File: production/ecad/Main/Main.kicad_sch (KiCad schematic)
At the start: 1 part, among them J1 61204021621

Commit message: touches to schem
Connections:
- net 3.3v: now reaches J1.1
- net 3.3v: now also J1.17
- net ANO_SW2: now reaches J1.10
- net LCD_CS: now reaches J1.11
- net ANO_SW3: now reaches J1.12
- net GND: now reaches J1.14
- net GND: now also J1.20, J1.25, J1.30, J1.34, J1.39, J1.6, J1.9
- net ANO_SW4: now reaches J1.16
- net ANO_SW5: now reaches J1.18
- net LCD_DIN: now reaches J1.19
- net 5v: now reaches J1.2
- net 5v: now also J1.4
- net MISO: now reaches J1.21
- net ANO_ENCB: now reaches J1.22
- net LCD_CLK: now reaches J1.23
- net ANO_ENCA: now reaches J1.24
- net LCD_DS: now reaches J1.27
- net LCD_BL: now reaches J1.29
- net SDA: now reaches J1.3
- net LCD_RST: now reaches J1.31
- net MTR_IN1: now reaches J1.32
- net MTR_IN1: now also J1.33
- net VBR_MTR_EN2: now reaches J1.37
- net VBR_MTR_EN2: now also J1.40
- net VBR_MTR_EN1: now reaches J1.38
- net SCL: now reaches J1.5
- net ANO_SW1: now reaches J1.8
- no-connect marks 0 -> 16
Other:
- added sheet ANO Dial (../Peripheral/Peripheral.kicad_sch)
- added sheet LCD (../LCD/LCD.kicad_sch)
- added sheet Motor (../Motor/Motor.kicad_sch)
- note added: "EXTERNAL GROUND PROVIDED FROM BMS/WALL"
- note added: "EXTERNAL VOLTAGE PROVIDED BY BMS/WALL"
- note added: "On pinout: - LCD screen - Motor driver - Rotary dial - Vibration motors"
- note added: "Still need: - weight sensor - ADC (maybe) -"
- moved on the sheet: J1

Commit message: schematic draft merged w neha
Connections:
- net VBR_MTR_EN2 is gone; now on net GND: J1.37, J1.40
- net MTR_DIR1: now reaches J1.26
- net MTR_EN1: now reaches J1.28
- net BMS/GNDEXT: now reaches J1.36
- no-connect marks 16 -> 13
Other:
- added sheet BMS (../BMS/BMS.kicad_sch)
- sheet Motor ports: added 3V3EXT, 5VEXT, MTR_DIR1, MTR_DIR2, MTR_EN1; removed 3.3VEXT, 6.5VEXT, MTR_IN2
- note removed: "EXTERNAL GROUND PROVIDED FROM BMS/WALL"
- note removed: "EXTERNAL VOLTAGE PROVIDED BY BMS/WALL"

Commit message: feedback from Billayyy
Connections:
- net GND: no longer J1.37, J1.40
- net BMS/GNDEXT renamed BMS/GND
- new net MTR_DIR2: J1.37
- new net VBR_MTR_EN2: J1.40
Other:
- sheet BMS ports: added GND; removed GNDEXT
- sheet Motor ports: added GND; removed GNDEXT

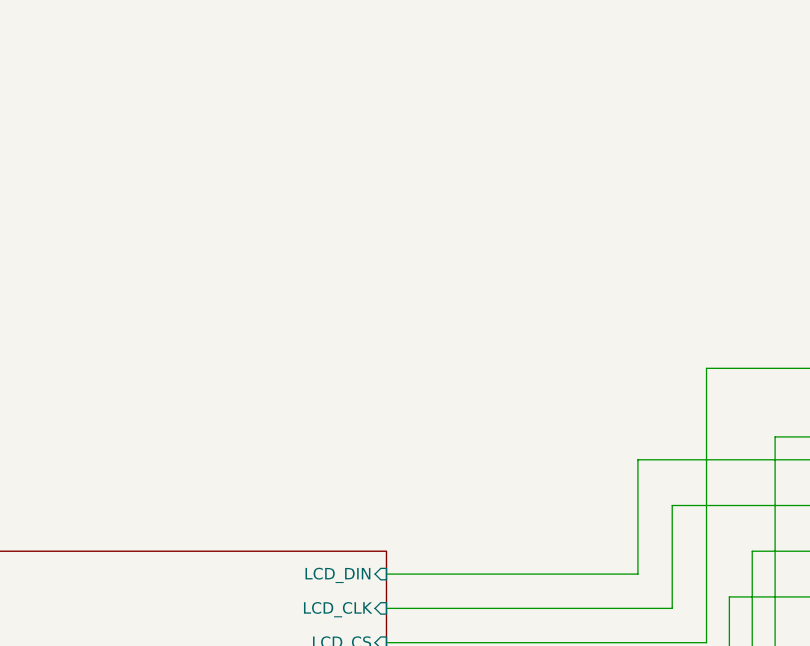
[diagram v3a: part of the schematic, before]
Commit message: added load cell blck but did not wire it up yet
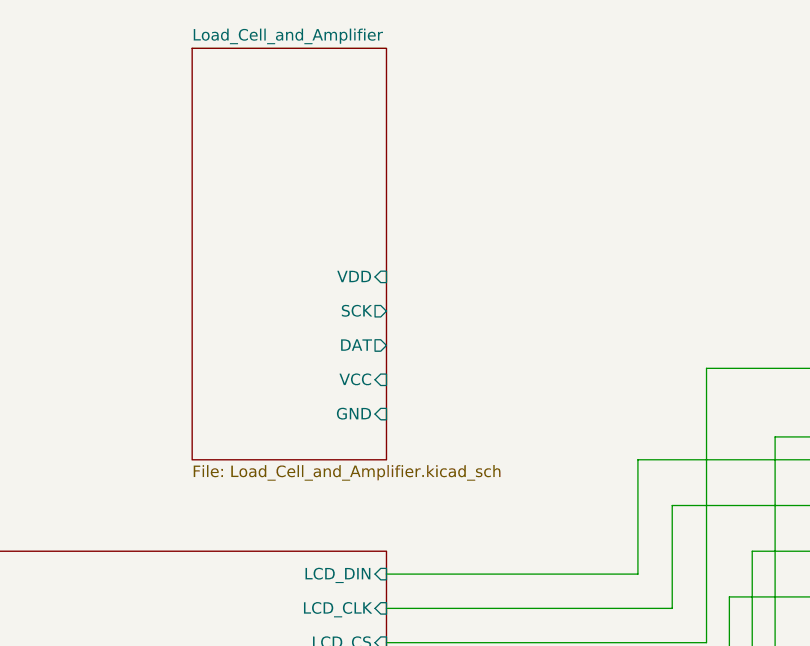
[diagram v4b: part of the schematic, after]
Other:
- added sheet Load_Cell_and_Amplifier (Load_Cell_and_Amplifier.kicad_sch)
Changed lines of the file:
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@@
+	)
+	(sheet
+		(at 44.45 17.78)
+		(size 21.59 45.72)
+		(fields_autoplaced yes)
+		(stroke
+			(width 0.1524)
+			(type solid)
+		)
+		(fill
+			(color 0 0 0 0.0000)
+		)
+		(property "Sheetname" "Load_Cell_and_Amplifier"
+			(at 44.45 17.0684 0)
+			(effects
+				(font
+					(size 1.27 1.27)
+				)
+				(justify left bottom)
+			)
+		)
+		(property "Sheetfile" "Load_Cell_and_Amplifier.kicad_sch"
+			(at 44.45 64.0846 0)
+			(effects
+				(font
+					(size 1.27 1.27)
+				)
+				(justify left top)
+			)
+		)
+		(pin "GND" input
+			(at 66.04 58.42 0)
+			(effects
+				(font
+					(size 1.27 1.27)
+				)
+				(justify right)
+			)
+		)
+		(pin "VCC" input
+			(at 66.04 54.61 0)
+			(effects
+				(font
+					(size 1.27 1.27)
+				)
+				(justify right)
+			)
+		)
+		(pin "DAT" output
+			(at 66.04 50.8 0)
+			(effects
+				(font
+					(size 1.27 1.27)
+				)
+				(justify right)
+			)
+		)
+		(pin "SCK" output
+			(at 66.04 46.99 0)
+			(effects
+				(font
+					(size 1.27 1.27)
+				)
+				(justify right)
+			)
+		)
+		(pin "VDD" input
+			(at 66.04 43.18 0)
+			(effects
+				(font
+					(size 1.27 1.27)
+				)
+				(justify right)
+			)
+		)
+		(instances
+			(project "Main"
+				(path "/a34d77bc-8f6a-417e-a206-3165e6c5c658"
+					(page "6")
+				)
+			)
+		)
 	)
 	(sheet

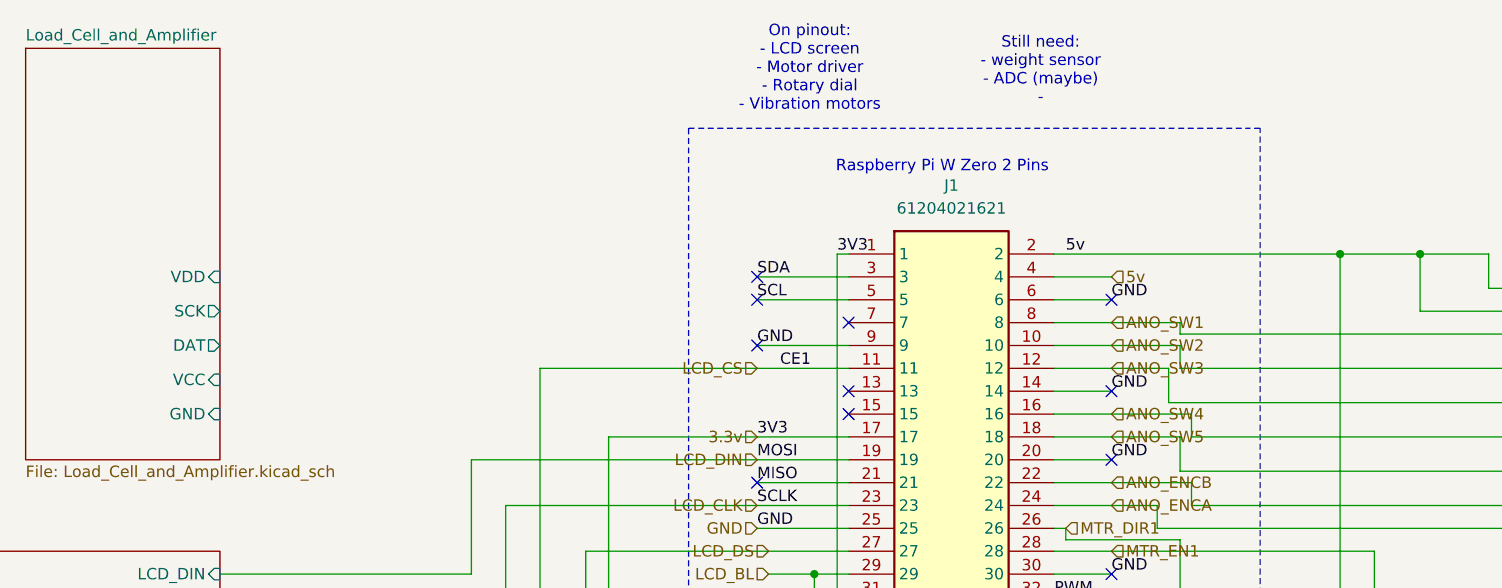
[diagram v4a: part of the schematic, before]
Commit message: connected to rabsperry pi
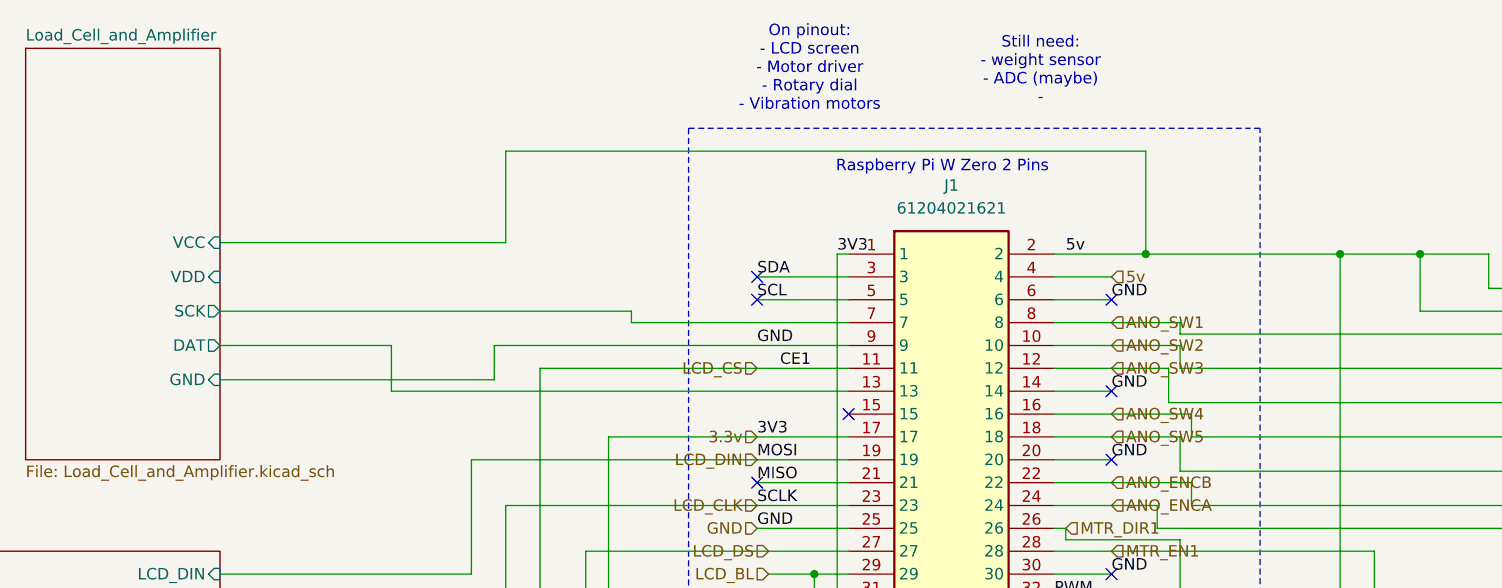
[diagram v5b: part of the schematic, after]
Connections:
- net Load_Cell_and_Amplifier/DAT: now also J1.13
- net Load_Cell_and_Amplifier/SCK: now also J1.7
- no-connect marks 13 -> 10
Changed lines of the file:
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@@
 	(paper "A4")
+	(junction
+		(at 168.91 40.64)
+		(diameter 0)
+		(color 0 0 0 0)
+	)
 	(junction
 		(at 162.56 138.43)
@@
 	)
 	(no_connect
-		(at 135.89 55.88)
-	)
-	(no_connect
-		(at 125.73 50.8)
-	)
-	(no_connect
 		(at 125.73 81.28)
 	)
@@
 	)
 	(no_connect
-		(at 135.89 48.26)
-	)
-	(no_connect
 		(at 165.1 63.5)
 	)
 	(wire
 		(pts
+			(xy 85.09 50.8) (xy 85.09 55.88)
+		)
+		(stroke
+			(width 0)
+			(type default)
+		)
+	)
+	(wire
+		(pts
 			(xy 120.65 121.92) (xy 190.5 121.92)
 		)
@@
 	(wire
 		(pts
+			(xy 66.04 46.99) (xy 111.76 46.99)
+		)
+		(stroke
+			(width 0)
+			(type default)
+		)
+	)
+	(wire
+		(pts
 			(xy 207.01 40.64) (xy 207.01 44.45)
 		)
@@
 	(wire
 		(pts
+			(xy 168.91 29.21) (xy 168.91 40.64)
+		)
+		(stroke
+			(width 0)
+			(type default)
+		)
+	)
+	(wire
+		(pts
 			(xy 190.5 40.64) (xy 199.39 40.64)
 		)
@@
 	(wire
 		(pts
-			(xy 125.73 50.8) (xy 135.89 50.8)
+			(xy 66.04 39.37) (xy 97.79 39.37)
 		)
 		(stroke
@@
 	(wire
 		(pts
+			(xy 97.79 39.37) (xy 97.79 29.21)
+		)
+		(stroke
+			(width 0)
+			(type default)
+		)
+	)
+	(wire
+		(pts
 			(xy 127 129.54) (xy 120.65 129.54)
 		)
@@
 	(wire
 		(pts
+			(xy 66.04 50.8) (xy 85.09 50.8)
+		)
+		(stroke
+			(width 0)
+			(type default)
+		)
+	)
+	(wire
+		(pts
 			(xy 66.04 87.63) (xy 104.14 87.63)
 		)
@@
 	(wire
 		(pts
+			(xy 85.09 55.88) (xy 135.89 55.88)
+		)
+		(stroke
+			(width 0)
+			(type default)
+		)
+	)
+	(wire
+		(pts
 			(xy 173.99 60.96) (xy 173.99 58.42)
 		)
@@
 	(wire
 		(pts
+			(xy 111.76 48.26) (xy 135.89 48.26)
+		)
+		(stroke
+			(width 0)
+			(type default)
+		)
+	)
+	(wire
+		(pts
 			(xy 209.55 64.77) (xy 172.72 64.77)
 		)
@@
 	(wire
 		(pts
+			(xy 168.91 40.64) (xy 190.5 40.64)
+		)
+		(stroke
+			(width 0)
+			(type default)
+		)
+	)
+	(wire
+		(pts
 			(xy 66.04 83.82) (xy 101.6 83.82)
 		)
@@
 	(wire
 		(pts
+			(xy 96.52 54.61) (xy 96.52 50.8)
+		)
+		(stroke
+			(width 0)
+			(type default)
+		)
+	)
+	(wire
+		(pts
+			(xy 97.79 29.21) (xy 168.91 29.21)
+		)
+		(stroke
+			(width 0)
+			(type default)
+		)
+	)
+	(wire
+		(pts
 			(xy 238.76 102.87) (xy 238.76 104.14)
 		)
@@
 	(wire
 		(pts
+			(xy 111.76 46.99) (xy 111.76 48.26)
+		)
+		(stroke
+			(width 0)
+			(type default)
+		)
+	)
+	(wire
+		(pts
 			(xy 172.72 53.34) (xy 172.72 50.8)
 		)
@@
 	(wire
 		(pts
+			(xy 96.52 50.8) (xy 135.89 50.8)
+		)
+		(stroke
+			(width 0)
+			(type default)
+		)
+	)
+	(wire
+		(pts
 			(xy 158.75 86.36) (xy 185.42 86.36)
 		)
@@
 	(wire
 		(pts
-			(xy 158.75 40.64) (xy 190.5 40.64)
+			(xy 158.75 40.64) (xy 168.91 40.64)
 		)
 		(stroke
@@
 		(pts
 			(xy 104.14 78.74) (xy 135.89 78.74)
+		)
+		(stroke
+			(width 0)
+			(type default)
+		)
+	)
+	(wire
+		(pts
+			(xy 66.04 54.61) (xy 96.52 54.61)
 		)
 		(stroke
@@
 		)
 		(pin "GND" input
-			(at 66.04 58.42 0)
+			(at 66.04 54.61 0)
 			(effects
 				(font
@@
 		)
 		(pin "VCC" input
-			(at 66.04 54.61 0)
+			(at 66.04 39.37 0)
 			(effects
 				(font

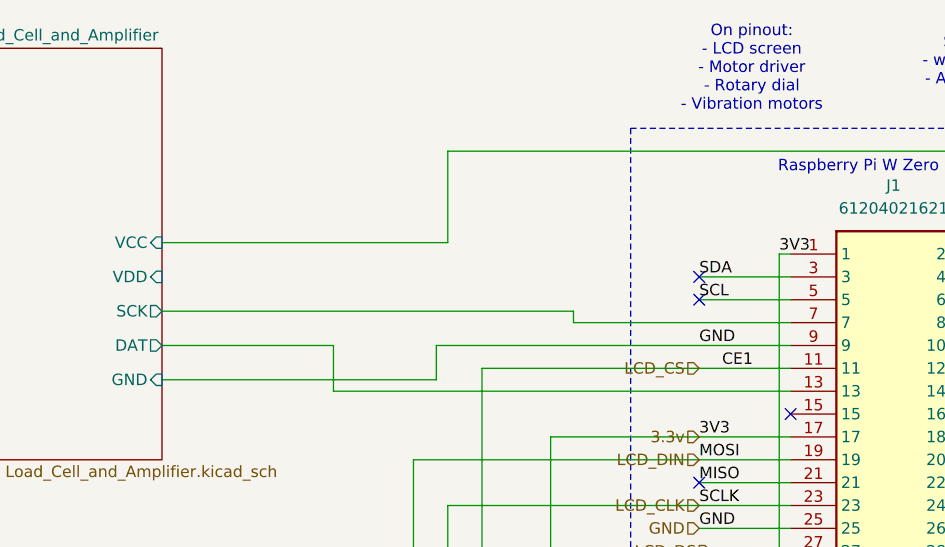
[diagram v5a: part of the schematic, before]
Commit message: Added new load cell connector, erased old thru hole connector from data side because we just have it on the pcb
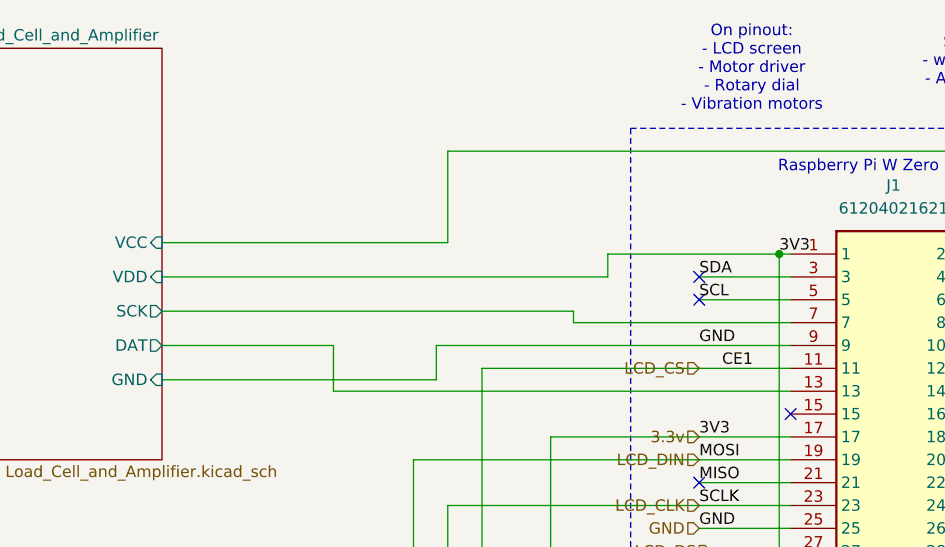
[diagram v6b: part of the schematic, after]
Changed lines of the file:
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@@
+	)
+	(junction
+		(at 134.62 40.64)
+		(diameter 0)
+		(color 0 0 0 0)
 	)
 	(junction
@@
 	(wire
 		(pts
+			(xy 115.57 40.64) (xy 134.62 40.64)
+		)
+		(stroke
+			(width 0)
+			(type default)
+		)
+	)
+	(wire
+		(pts
 			(xy 199.39 46.99) (xy 199.39 40.64)
 		)
@@
 	(wire
 		(pts
+			(xy 115.57 43.18) (xy 115.57 40.64)
+		)
+		(stroke
+			(width 0)
+			(type default)
+		)
+	)
+	(wire
+		(pts
 			(xy 168.91 29.21) (xy 168.91 40.64)
 		)
@@
 		)
 		(stroke
+			(width 0)
+			(type default)
+		)
+	)
+	(wire
+		(pts
+			(xy 66.04 43.18) (xy 115.57 43.18)
+		)
+		(stroke

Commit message: feedback
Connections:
- net 3.3v renamed +3.3V
- net 5v renamed +5V
- net BMS/GND: no longer names the net of J1.36
- net Load_Cell_and_Amplifier/DAT renamed W_DAT
- net Load_Cell_and_Amplifier/SCK renamed W_SCK
- no-connect marks 10 -> 9
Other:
- sheet ANO Dial: file ../Peripheral/Peripheral.kicad_sch -> ../ANO-DIAL/ANO-DIAL.kicad_sch
- sheet Load_Cell_and_Amplifier: file Load_Cell_and_Amplifier.kicad_sch -> ../LOAD-CELL/LOAD-CELL.kicad_sch
